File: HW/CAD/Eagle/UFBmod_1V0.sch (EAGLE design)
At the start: 87 parts, among them U101 DIGILENT_CMOD_A7, U301 MAX5217, U401 AT86RF215-ZU, U411 ASVTX-13-D-26.000MHZ-I05-T, U511 PE4259, U521 RFX1010, U581 B39871B3440U410, U611 TPS62056DGSR, X221 TTE_EN11-HSM, X591 ANTENNATINY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

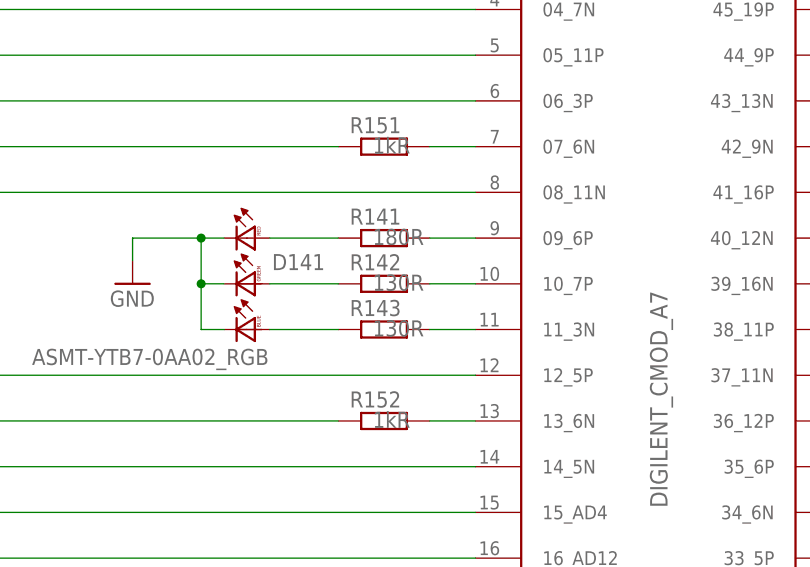
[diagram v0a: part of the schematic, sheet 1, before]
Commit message: HW_1V0 - CAD/Eagle - LED resistors changed
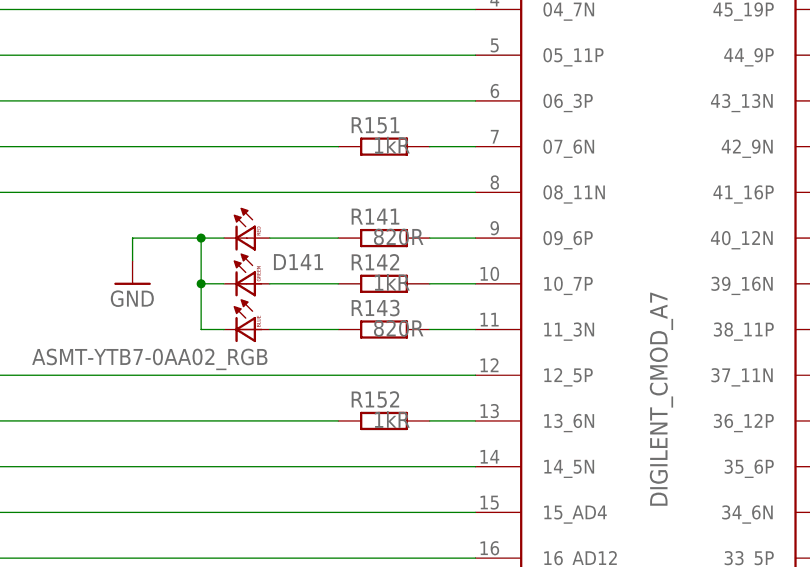
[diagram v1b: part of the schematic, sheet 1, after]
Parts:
- R141: value 180R -> 820R
- R142: value 130R -> 1kR
- R143: value 130R -> 820R
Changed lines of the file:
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@@
 <part name="R734" library="df4iah_rcl" deviceset="R-EU_" device="R0402" value="100R"/>
 <part name="R733" library="df4iah_rcl" deviceset="R-EU_" device="R0402" value="100R"/>
-<part name="R141" library="df4iah_rcl" deviceset="R-EU_" device="R0402" value="180R"/>
-<part name="R142" library="df4iah_rcl" deviceset="R-EU_" device="R0402" value="130R"/>
-<part name="R143" library="df4iah_rcl" deviceset="R-EU_" device="R0402" value="130R"/>
+<part name="R141" library="df4iah_rcl" deviceset="R-EU_" device="R0402" value="820R"/>
+<part name="R142" library="df4iah_rcl" deviceset="R-EU_" device="R0402" value="1kR"/>
+<part name="R143" library="df4iah_rcl" deviceset="R-EU_" device="R0402" value="820R"/>
 <part name="D141" library="df4iah_led" deviceset="ASMT-YTB7-0AA02_RGB" device=""/>
 <part name="GND141" library="df4iah_supply" deviceset="GND" device=""/>
